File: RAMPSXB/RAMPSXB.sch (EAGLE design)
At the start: 97 parts, among them CN1 1X4-BIG, CN2 1X4-BIG, CN3 1X4-BIG, CN4 1X4-BIG, CN5 1X4-BIG, CN6 1X4-BIG, CN7 1X4-BIG, CN8 1X4-BIG, CN9 1X4-BIG, J1 1X2-3.5MM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

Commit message: Expanded Traces, Fixed Fonts
Changed Fonts to Vector, so they come out in the right place. Expanded
power traces.
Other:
- note added: "(C) Scott Ziv"
- note added: "GPLv3"
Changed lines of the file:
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@@
 <text x="-20.32" y="-5.08" size="5.08" layer="108">CAPACITORS</text>
 <text x="-20.32" y="-142.24" size="5.08" layer="108">HC-05</text>
-<text x="-35.56" y="50.8" size="6.4516" layer="91">RAMPSXB</text>
+<text x="93.98" y="50.8" size="6.4516" layer="91">RAMPSXB</text>
 <text x="177.8" y="50.8" size="6.4516" layer="91">http://reprap.org/wiki/RAMPSXB</text>
+<text x="-63.5" y="50.8" size="3.81" layer="91">(C) Scott Ziv</text>
+<text x="-10.16" y="50.8" size="3.81" layer="91">GPLv3</text>
 </plain>
 <instances>
@@
 <wire x1="264.16" y1="-71.12" x2="264.16" y2="-40.64" width="0.1524" layer="91"/>
 <wire x1="264.16" y1="-40.64" x2="264.16" y2="43.18" width="0.1524" layer="91"/>
-<wire x1="264.16" y1="43.18" x2="104.14" y2="43.18" width="0.1524" layer="91"/>
+<wire x1="264.16" y1="43.18" x2="162.56" y2="43.18" width="0.1524" layer="91"/>
+<wire x1="162.56" y1="43.18" x2="104.14" y2="43.18" width="0.1524" layer="91"/>
 <wire x1="104.14" y1="43.18" x2="104.14" y2="-71.12" width="0.1524" layer="91"/>
 <wire x1="104.14" y1="-71.12" x2="121.92" y2="-71.12" width="0.1524" layer="91"/>
@@
 <wire x1="-78.74" y1="43.18" x2="-78.74" y2="60.96" width="0.1524" layer="91"/>
 <junction x="-78.74" y="43.18"/>
-<wire x1="-78.74" y1="60.96" x2="337.82" y2="60.96" width="0.1524" layer="91"/>
+<wire x1="-78.74" y1="60.96" x2="22.86" y2="60.96" width="0.1524" layer="91"/>
+<wire x1="22.86" y1="60.96" x2="162.56" y2="60.96" width="0.1524" layer="91"/>
+<wire x1="162.56" y1="60.96" x2="337.82" y2="60.96" width="0.1524" layer="91"/>
 <wire x1="337.82" y1="60.96" x2="337.82" y2="43.18" width="0.1524" layer="91"/>
 <junction x="337.82" y="43.18"/>
-</segment>
-</net>
+<wire x1="22.86" y1="43.18" x2="22.86" y2="60.96" width="0.1524" layer="91"/>
+<junction x="22.86" y="60.96"/>
+<wire x1="162.56" y1="43.18" x2="162.56" y2="60.96" width="0.1524" layer="91"/>
+<junction x="162.56" y="43.18"/>
+<junction x="162.56" y="60.96"/>
+</segment>
+</net>

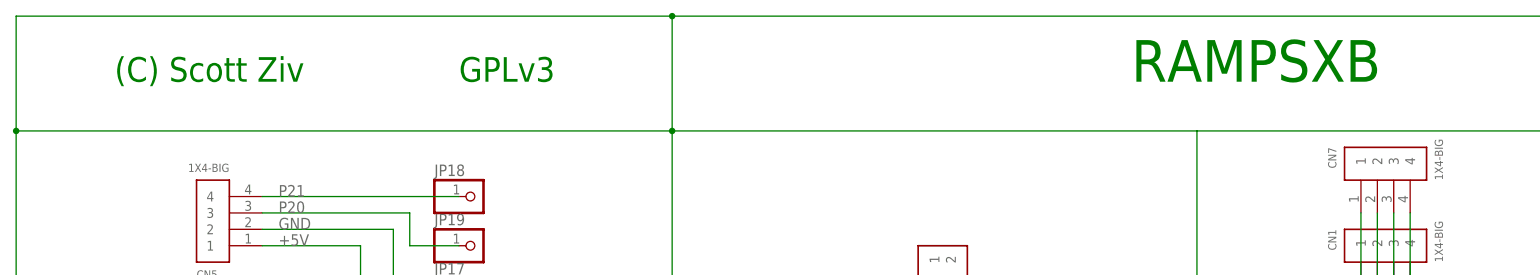
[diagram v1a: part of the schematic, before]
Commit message: Incremented Version number and added a bigger OSHW Logo to fill in the empty space
Hopefully, this should be close to the final version
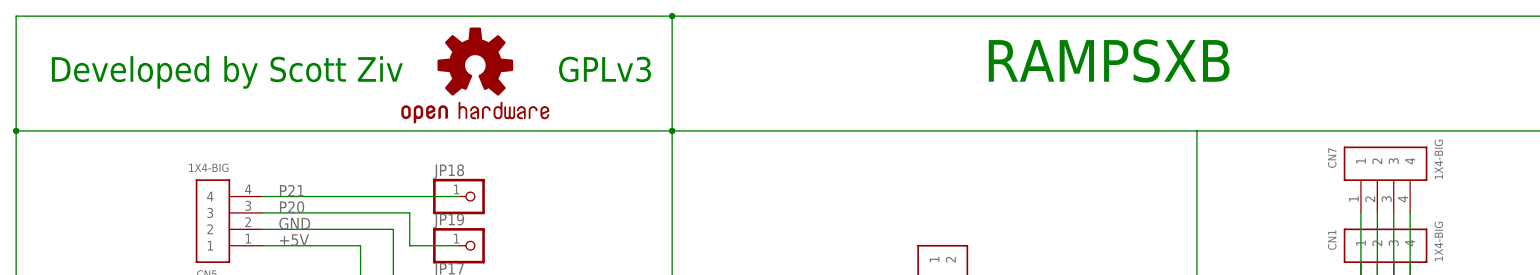
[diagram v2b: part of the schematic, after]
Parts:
- added LOGO2: OSHW-LOGOL, SparkFun-Aesthetics:OSHW-LOGOL
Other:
- note added: "Developed by Scott Ziv"
- note removed: "(C) Scott Ziv"
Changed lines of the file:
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@@
 <layer number="112" name="tSilk" color="7" fill="1" visible="no" active="yes"/>
 <layer number="113" name="ReferenceLS" color="7" fill="1" visible="no" active="no"/>
+<layer number="114" name="Badge_Outline" color="7" fill="1" visible="no" active="yes"/>
+<layer number="115" name="ReferenceISLANDS" color="7" fill="1" visible="no" active="yes"/>
 <layer number="116" name="Patch_BOT" color="9" fill="4" visible="yes" active="yes"/>
 <layer number="118" name="Rect_Pads" color="7" fill="1" visible="no" active="no"/>
@@
 <part name="Q1" library="MyLibrary" deviceset="PSMN7R0-30YLC" device=""/>
 <part name="Q4" library="MyLibrary" deviceset="PSMN7R0-30YLC" device=""/>
+<part name="LOGO2" library="SparkFun-Aesthetics" deviceset="OSHW-LOGO" device="L"/>
 </parts>
 <sheets>
@@
 <text x="-20.32" y="-5.08" size="5.08" layer="108">CAPACITORS</text>
 <text x="-20.32" y="-142.24" size="5.08" layer="108">HC-05</text>
-<text x="93.98" y="50.8" size="6.4516" layer="91">RAMPSXB</text>
+<text x="71.12" y="50.8" size="6.4516" layer="91">RAMPSXB</text>
 <text x="177.8" y="50.8" size="6.4516" layer="91">http://reprap.org/wiki/RAMPSXB</text>
-<text x="-63.5" y="50.8" size="3.81" layer="91">(C) Scott Ziv</text>
-<text x="-10.16" y="50.8" size="3.81" layer="91">GPLv3</text>
+<text x="-73.66" y="50.8" size="3.81" layer="91">Developed by Scott Ziv</text>
+<text x="5.08" y="50.8" size="3.81" layer="91">GPLv3</text>
 </plain>
 <instances>
@@
 <attribute name="VALUE" x="314.706" y="-61.214" size="1.27" layer="96" rot="R180"/>
 </instance>
+<instance part="LOGO2" gate="G$1" x="-7.62" y="53.34"/>
 </instances>
 <busses>

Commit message: Fixed some issues with V2.1, and updated gerbers
fixed some stuff with V2.1 and corrected some issues
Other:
- note added: "Developed by SZiv"
- note removed: "Developed by Scott Ziv"
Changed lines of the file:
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@@
 <text x="71.12" y="50.8" size="6.4516" layer="91">RAMPSXB</text>
 <text x="177.8" y="50.8" size="6.4516" layer="91">http://reprap.org/wiki/RAMPSXB</text>
-<text x="-73.66" y="50.8" size="3.81" layer="91">Developed by Scott Ziv</text>
+<text x="-73.66" y="50.8" size="3.81" layer="91">Developed by SZiv</text>
 <text x="5.08" y="50.8" size="3.81" layer="91">GPLv3</text>
 </plain>
